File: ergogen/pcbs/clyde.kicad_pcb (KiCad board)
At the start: 2 copper layers, 116.7 x 83.3 mm, 61 parts

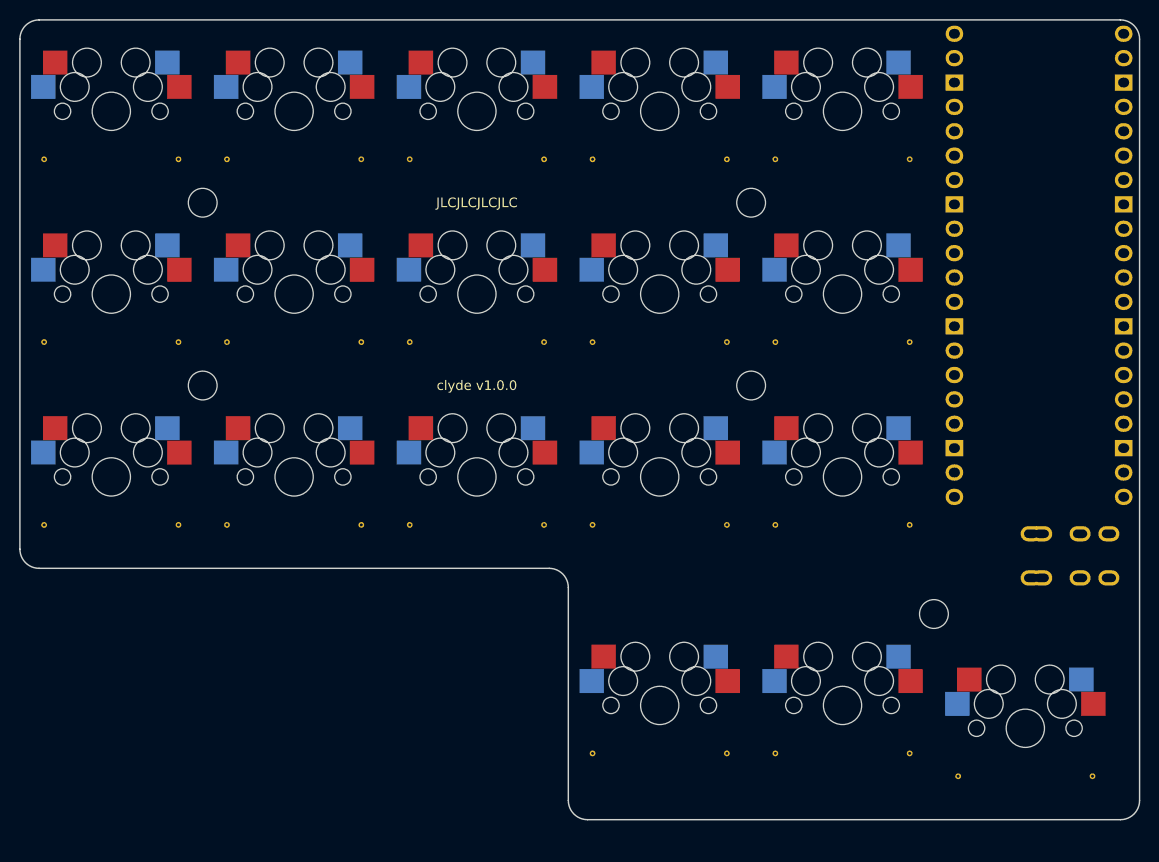
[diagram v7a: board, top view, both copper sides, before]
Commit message: rj45, PCB solder nuts, acrylic bottom plate
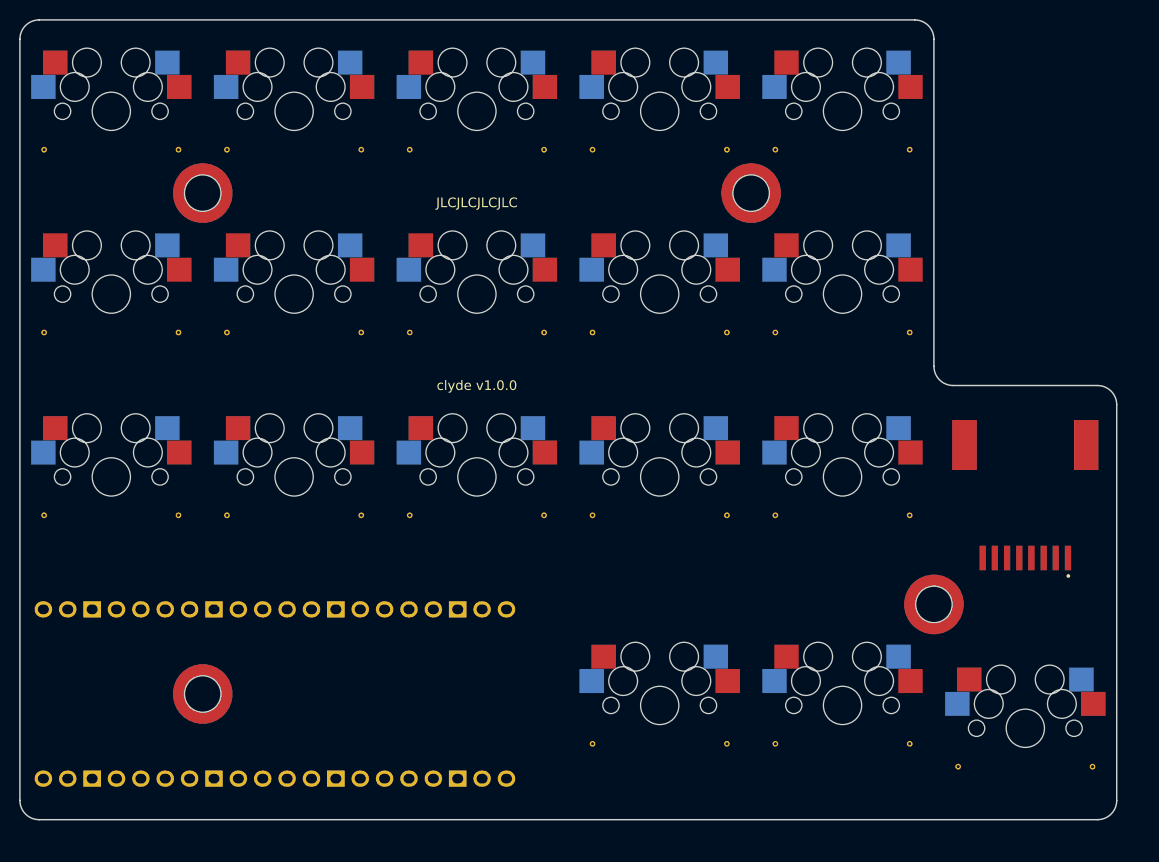
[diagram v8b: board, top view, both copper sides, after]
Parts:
- removed the ? at (238.1, 166.7)
- removed the ? at (161.9, 123.8)
- removed the ? at (161.9, 142.9)
- removed the ? at (219.1, 123.8)
- removed the ? at (219.1, 142.9)
- removed the REF** at (145.4, 157.4)
- removed the REF** at (202.6, 157.4)
- removed the REF** at (202.6, 138.3)
- removed the REF** at (202.6, 119.3)
- removed the REF** at (221.6, 157.4)
- removed the REF** at (221.6, 138.3)
- removed the REF** at (221.6, 119.3)
- removed the REF** at (202.6, 181.2)
- removed the REF** at (221.6, 181.2)
- removed the REF** at (240.7, 183.6)
- removed the REF** at (159.4, 157.4)
- removed the REF** at (145.4, 138.3)
- removed the REF** at (159.4, 138.3)
- removed the REF** at (159.4, 119.3)
- removed the REF** at (178.5, 157.4)
- removed the REF** at (178.5, 138.3)
- removed the REF** at (178.5, 119.3)
- removed the REF** at (197.5, 157.4)
- removed the REF** at (197.5, 138.3)
- removed the REF** at (197.5, 119.3)
- removed the REF** at (216.6, 157.4)
- removed the REF** at (216.6, 138.3)
- removed the REF** at (145.4, 119.3)
- removed the REF** at (216.6, 119.3)
- removed the REF** at (235.6, 157.4)
- removed the REF** at (235.6, 138.3)
- removed the REF** at (235.6, 119.3)
- removed the REF** at (216.6, 181.2)
- removed the REF** at (235.6, 181.2)
- removed the REF** at (254.7, 183.6)
- removed the REF** at (164.5, 157.4)
- removed the REF** at (164.5, 138.3)
- removed the REF** at (164.5, 119.3)
- removed the REF** at (183.5, 157.4)
- removed the REF** at (183.5, 138.3)
- removed the REF** at (183.5, 119.3)
- removed TRRS1: TRRS-PJ-320A-dual, TRRS-PJ-320A-dual
- added ?: , 44144-0003, F.Cu at (247.7, 160.0)
- added ?: , SMTSO2020MTJ,  at (161.9, 122.8)
- added ?: , SMTSO2020MTJ,  at (219.1, 122.8)
- added ?: , SMTSO2020MTJ,  at (238.1, 165.7)
- added ?: , SMTSO2020MTJ,  at (161.9, 175.0)
- added REF**: VIA-0.6mm, VIA-0.6mm, F.Cu at (145.4, 156.4)
- added REF**: VIA-0.6mm, VIA-0.6mm, F.Cu at (202.6, 156.4)
- added REF**: VIA-0.6mm, VIA-0.6mm, F.Cu at (202.6, 137.3)
- added REF**: VIA-0.6mm, VIA-0.6mm, F.Cu at (202.6, 118.3)
- added REF**: VIA-0.6mm, VIA-0.6mm, F.Cu at (221.6, 156.4)
- added REF**: VIA-0.6mm, VIA-0.6mm, F.Cu at (221.6, 137.3)
- added REF**: VIA-0.6mm, VIA-0.6mm, F.Cu at (221.6, 118.3)
- added REF**: VIA-0.6mm, VIA-0.6mm, F.Cu at (202.6, 180.2)
- added REF**: VIA-0.6mm, VIA-0.6mm, F.Cu at (221.6, 180.2)
- added REF**: VIA-0.6mm, VIA-0.6mm, F.Cu at (240.7, 182.6)
- added REF**: VIA-0.6mm, VIA-0.6mm, F.Cu at (159.4, 156.4)
- added REF**: VIA-0.6mm, VIA-0.6mm, F.Cu at (145.4, 137.3)
- added REF**: VIA-0.6mm, VIA-0.6mm, F.Cu at (159.4, 137.3)
- added REF**: VIA-0.6mm, VIA-0.6mm, F.Cu at (159.4, 118.3)
- added REF**: VIA-0.6mm, VIA-0.6mm, F.Cu at (178.5, 156.4)
- added REF**: VIA-0.6mm, VIA-0.6mm, F.Cu at (178.5, 137.3)
- added REF**: VIA-0.6mm, VIA-0.6mm, F.Cu at (178.5, 118.3)
- added REF**: VIA-0.6mm, VIA-0.6mm, F.Cu at (197.5, 156.4)
- added REF**: VIA-0.6mm, VIA-0.6mm, F.Cu at (197.5, 137.3)
- added REF**: VIA-0.6mm, VIA-0.6mm, F.Cu at (197.5, 118.3)
- added REF**: VIA-0.6mm, VIA-0.6mm, F.Cu at (216.6, 156.4)
- added REF**: VIA-0.6mm, VIA-0.6mm, F.Cu at (216.6, 137.3)
- added REF**: VIA-0.6mm, VIA-0.6mm, F.Cu at (145.4, 118.3)
- added REF**: VIA-0.6mm, VIA-0.6mm, F.Cu at (216.6, 118.3)
- added REF**: VIA-0.6mm, VIA-0.6mm, F.Cu at (235.6, 156.4)
- added REF**: VIA-0.6mm, VIA-0.6mm, F.Cu at (235.6, 137.3)
- added REF**: VIA-0.6mm, VIA-0.6mm, F.Cu at (235.6, 118.3)
- added REF**: VIA-0.6mm, VIA-0.6mm, F.Cu at (216.6, 180.2)
- added REF**: VIA-0.6mm, VIA-0.6mm, F.Cu at (235.6, 180.2)
- added REF**: VIA-0.6mm, VIA-0.6mm, F.Cu at (254.7, 182.6)
- added REF**: VIA-0.6mm, VIA-0.6mm, F.Cu at (164.5, 156.4)
- added REF**: VIA-0.6mm, VIA-0.6mm, F.Cu at (164.5, 137.3)
- added REF**: VIA-0.6mm, VIA-0.6mm, F.Cu at (164.5, 118.3)
- added REF**: VIA-0.6mm, VIA-0.6mm, F.Cu at (183.5, 156.4)
- added REF**: VIA-0.6mm, VIA-0.6mm, F.Cu at (183.5, 137.3)
- added REF**: VIA-0.6mm, VIA-0.6mm, F.Cu at (183.5, 118.3)
- U0: footprint RPi_Pico_TH_oval_face_up -> RPi_Pico_TH_oval_face_down
- moved U0 91.3 mm to (169.5, 175.0), turned to 90 degrees
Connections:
- U0 pad 10: matrix_inner_home -> matrix_middle_home
- U0 pad 11: matrix_inner_bottom -> matrix_middle_bottom
- U0 pad 12: matrix_ring_bottom -> matrix_index_top
- U0 pad 14: matrix_ring_home -> matrix_index_home
- U0 pad 15: matrix_ring_top -> matrix_index_bottom
- U0 pad 16: matrix_middle_top -> matrix_inner_bottom
- U0 pad 17: matrix_middle_home -> matrix_inner_home
- U0 pad 19: matrix_middle_bottom -> matrix_inner_top
- U0 pad 22: thumb_far_mods -> GP17
- U0 pad 24: thumb_middle_mods -> thumb_far_mods
- U0 pad 25: thumb_near_mods -> thumb_middle_mods
- U0 pad 26: GP20 -> thumb_near_mods
- U0 pad 5: matrix_index_bottom -> matrix_ring_top
- U0 pad 6: matrix_index_home -> matrix_ring_home
- U0 pad 7: matrix_index_top -> matrix_ring_bottom
- U0 pad 9: matrix_inner_top -> matrix_middle_top
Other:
- board size 116.7 x 83.3 mm -> 114.3 x 83.3 mm
